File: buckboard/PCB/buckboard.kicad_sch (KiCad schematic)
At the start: 159 parts, among them J1 Conn_01x05, SW1 SW_Push, SW10 SW_Push, SW100_1.25 SW_Push, SW101 SW_Push, SW102 SW_Push, SW103_1.25 SW_Push, SW104_1.25 SW_Push, SW105_1.25 SW_Push, SW106_1.5 SW_Push, SW11 SW_Push, SW12 SW_Push, SW13 SW_Push, SW17 SW_Push, SW18 SW_Push, SW19 SW_Push, SW2 SW_Push, SW20 SW_Push, SW21 SW_Push, SW22 SW_Push, SW23 SW_Push, SW24 SW_Push, SW25 SW_Push, SW26 SW_Push, SW27 SW_Push, SW28 SW_Push, SW29 SW_Push, SW3 SW_Push, SW30_2 SW_Push, SW4 SW_Push, SW5 SW_Push, SW58_1.5 SW_Push, SW59 SW_Push, SW6 SW_Push, SW60 SW_Push, SW61 SW_Push, SW62 SW_Push, SW63 SW_Push, SW64 SW_Push, SW65 SW_Push, SW66 SW_Push, SW67 SW_Push, SW68 SW_Push, SW69 SW_Push, SW7 SW_Push, SW70 SW_Push, SW71 SW_Push, SW71_1.75 SW_Push, SW72 SW_Push, SW73 SW_Push, SW74 SW_Push, SW75 SW_Push, SW76 SW_Push, SW77 SW_Push, SW78 SW_Push, SW79 SW_Push, SW8 SW_Push, SW80 SW_Push, SW81 SW_Push, SW82 SW_Push, SW83 SW_Push, SW84_enter1 SW_Push, SW85_1.25 SW_Push, SW86 SW_Push, SW87 SW_Push, SW88 SW_Push, SW89 SW_Push, SW9 SW_Push, SW90 SW_Push, SW91 SW_Push, SW92 SW_Push, SW93 SW_Push, SW94 SW_Push, SW95 SW_Push, SW96 SW_Push, SW97_2.75 SW_Push, SW98_1.5 SW_Push, SW99_1.25 SW_Push

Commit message: created pcb model and wired it up + added secondary rotary encoder
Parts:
- added SW14: RotaryEncoder, Rotary_Encoder:RotaryEncoder_Alps_EC12E_Vertical_H20mm, symbol Device:RotaryEncoder
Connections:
- net GND: now also SW14.C
- net EC12A: now reaches A1.32 (GPIO27_ADC1)
- net EC12A: now also SW14.A
- net EC12B: now reaches A1.34 (GPIO28_ADC2)
- net EC12B: now also SW14.B
- net row1 renamed p18
- net row2 renamed p19
- net row3 renamed p20
- net row4 renamed p21
- net row5 renamed p22
- net row6 renamed p26
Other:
- moved on the sheet: OLED DISPLAY1, SWvol1

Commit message: updated pcb to have joystick module support (- 1 rotary encoder)+ gerber
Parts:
- removed SW14: RotaryEncoder, Rotary_Encoder:RotaryEncoder_Alps_EC12E_Vertical_H20mm, symbol Device:RotaryEncoder
- J1: footprint Connector_PinHeader_1.00mm:PinHeader_1x05_P1.00mm_Vertical -> Connector_PinSocket_2.00mm:PinSocket_1x05_P2.00mm_Horizontal
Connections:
- net EC12A is gone; now on net VRx: A1.32 (GPIO27_ADC1)
- net EC12B is gone; now on net VRy: A1.34 (GPIO28_ADC2)
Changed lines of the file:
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@@
 	(wire
 		(pts
-			(xy 504.19 82.55) (xy 518.16 82.55)
-		)
-		(stroke
-			(width 0)
-			(type default)
-		)
-	)
-	(wire
-		(pts
 			(xy 227.33 156.21) (xy 227.33 173.99)
 		)
@@
 		)
 	)
-	(global_label "EC12A"
-		(shape input)
-		(at 397.51 29.21 0)
-		(fields_autoplaced yes)
-		(effects
-			(font
-				(size 1.27 1.27)
-			)
-			(justify left)
-		)
-		(property "Intersheetrefs" "${INTERSHEET_REFS}"
-			(at 406.4218 29.21 0)
-			(hide yes)
-			(show_name no)
-			(do_not_autoplace no)
-			(effects
-				(font
-					(size 1.27 1.27)
-				)
-				(justify left)
-			)
-		)
-	)
 	(global_label "row4"
 		(shape input)
@@
 		)
 	)
+	(global_label "VRy"
+		(shape input)
+		(at 397.51 31.75 0)
+		(fields_autoplaced yes)
+		(effects
+			(font
+				(size 1.27 1.27)
+			)
+			(justify left)
+		)
+		(property "Intersheetrefs" "${INTERSHEET_REFS}"
+			(at 403.8214 31.75 0)
+			(hide yes)
+			(show_name no)
+			(do_not_autoplace no)
+			(effects
+				(font
+					(size 1.27 1.27)
+				)
+				(justify left)
+			)
+		)
+	)
 	(global_label "p18"
 		(shape input)
@@
 		)
 	)
-	(global_label "EC12A"
-		(shape input)
-		(at 518.16 80.01 180)
-		(fields_autoplaced yes)
-		(effects
-			(font
-				(size 1.27 1.27)
-			)
-			(justify right)
-		)
-		(property "Intersheetrefs" "${INTERSHEET_REFS}"
-			(at 509.2482 80.01 0)
-			(hide yes)
-			(show_name no)
-			(do_not_autoplace no)
-			(effects
-				(font
-					(size 1.27 1.27)
-				)
-				(justify right)
-			)
-		)
-	)
 	(global_label "col10"
 		(shape input)
@@
 		)
 	)
-	(global_label "EC12B"
-		(shape input)
-		(at 518.16 85.09 180)
-		(fields_autoplaced yes)
-		(effects
-			(font
-				(size 1.27 1.27)
-			)
-			(justify right)
-		)
-		(property "Intersheetrefs" "${INTERSHEET_REFS}"
-			(at 509.0668 85.09 0)
-			(hide yes)
-			(show_name no)
-			(do_not_autoplace no)
-			(effects
-				(font
-					(size 1.27 1.27)
-				)
-				(justify right)
-			)
-		)
-	)
 	(global_label "col3"
 		(shape input)
@@
 		)
 	)
+	(global_label "VRx"
+		(shape input)
+		(at 397.51 29.21 0)
+		(fields_autoplaced yes)
+		(effects
+			(font
+				(size 1.27 1.27)
+			)
+			(justify left)
+		)
+		(property "Intersheetrefs" "${INTERSHEET_REFS}"
+			(at 403.8819 29.21 0)
+			(hide yes)
+			(show_name no)
+			(do_not_autoplace no)
+			(effects
+				(font
+					(size 1.27 1.27)
+				)
+				(justify left)
+			)
+		)
+	)
 	(global_label "col2"
 		(shape input)
@@
 		)
 	)
-	(global_label "EC12B"
-		(shape input)
-		(at 397.51 31.75 0)
-		(fields_autoplaced yes)
-		(effects
-			(font
-				(size 1.27 1.27)
-			)
-			(justify left)
-		)
-		(property "Intersheetrefs" "${INTERSHEET_REFS}"
-			(at 406.6032 31.75 0)
-			(hide yes)
-			(show_name no)
-			(do_not_autoplace no)
-			(effects
-				(font
-					(size 1.27 1.27)
-				)
-				(justify left)
-			)
-		)
-	)
 	(global_label "col14"
 		(shape input)
@@
 	)
 	(symbol
-		(lib_id "power:GND")
-		(at 504.19 82.55 0)
-		(unit 1)
-		(body_style 1)
-		(exclude_from_sim no)
-		(in_bom yes)
-		(on_board yes)
-		(in_pos_files yes)
-		(dnp no)
-		(fields_autoplaced yes)
-		(property "Reference" "#PWR09"
-			(at 504.19 88.9 0)
-			(hide yes)
-			(show_name no)
-			(do_not_autoplace no)
-			(effects
-				(font
-					(size 1.27 1.27)
-				)
-			)
-		)
-		(property "Value" "GND"
-			(at 504.19 87.63 0)
-			(show_name no)
-			(do_not_autoplace no)
-			(effects
-				(font
-					(size 1.27 1.27)
-				)
-			)
-		)
-		(property "Footprint" ""
-			(at 504.19 82.55 0)
-			(hide yes)
-			(show_name no)
-			(do_not_autoplace no)
-			(effects
-				(font
-					(size 1.27 1.27)
-				)
-			)
-		)
-		(property "Datasheet" ""
-			(at 504.19 82.55 0)
-			(hide yes)
-			(show_name no)
-			(do_not_autoplace no)
-			(effects
-				(font
-					(size 1.27 1.27)
-				)
-			)
-		)
-		(property "Description" "Power symbol creates a global label with name \"GND\" , ground"
-			(at 504.19 82.55 0)
-			(hide yes)
-			(show_name no)
-			(do_not_autoplace no)
-			(effects
-				(font
-					(size 1.27 1.27)
-				)
-			)
-		)
-		(pin "1"
-		)
-		(instances
-			(project "buckboard"
-				(path "/92392aa8-3793-4fda-a137-246c9c5a2323"
-					(reference "#PWR09")
-					(unit 1)
-				)
-			)
-		)
-	)
-	(symbol
 		(lib_id "Switch:SW_Push")
 		(at 278.13 80.01 180)
@@
 	)
 	(symbol
-		(lib_id "Device:RotaryEncoder")
-		(at 525.78 82.55 0)
-		(unit 1)
-		(body_style 1)
-		(exclude_from_sim no)
-		(in_bom yes)
-		(on_board yes)
-		(in_pos_files yes)
-		(dnp no)
-		(fields_autoplaced yes)
-		(property "Reference" "SW14"
-			(at 532.13 81.2799 0)
-			(show_name no)
-			(do_not_autoplace no)
-			(effects
-				(font
-					(size 1.27 1.27)
-				)
-				(justify left)
-			)
-		)
-		(property "Value" "RotaryEncoder"
-			(at 532.13 83.8199 0)
-			(show_name no)
-			(do_not_autoplace no)
-			(effects
-				(font
-					(size 1.27 1.27)
-				)
-				(justify left)
-			)
-		)
-		(property "Footprint" "Rotary_Encoder:RotaryEncoder_Alps_EC12E_Vertical_H20mm"
-			(at 521.97 78.486 0)
-			(hide yes)
-			(show_name no)
-			(do_not_autoplace no)
-			(effects
-				(font
-					(size 1.27 1.27)
-				)
-			)
-		)
-		(property "Datasheet" ""
-			(at 525.78 75.946 0)
-			(hide yes)
-			(show_name no)
-			(do_not_autoplace no)
-			(effects
-				(font
-					(size 1.27 1.27)
-				)
-			)
-		)
-		(property "Description" "Rotary encoder, dual channel, incremental quadrate outputs"
-			(at 525.78 82.55 0)
-			(hide yes)
-			(show_name no)
-			(do_not_autoplace no)
-			(effects
-				(font
-					(size 1.27 1.27)
-				)
-			)
-		)
-		(pin "C"
-		)
-		(pin "B"
-		)
-		(pin "A"
-		)
-		(instances
-			(project "buckboard"
-				(path "/92392aa8-3793-4fda-a137-246c9c5a2323"
-					(reference "SW14")
-					(unit 1)
-				)
-			)
-		)
-	)
-	(symbol
 		(lib_id "Switch:SW_Push")
 		(at 293.37 80.01 180)
@@
 			)
 		)
-		(property "Footprint" "Connector_PinHeader_1.00mm:PinHeader_1x05_P1.00mm_Vertical"
+		(property "Footprint" "Connector_PinSocket_2.00mm:PinSocket_1x05_P2.00mm_Horizontal"
 			(at 535.94 161.29 0)
 			(hide yes)

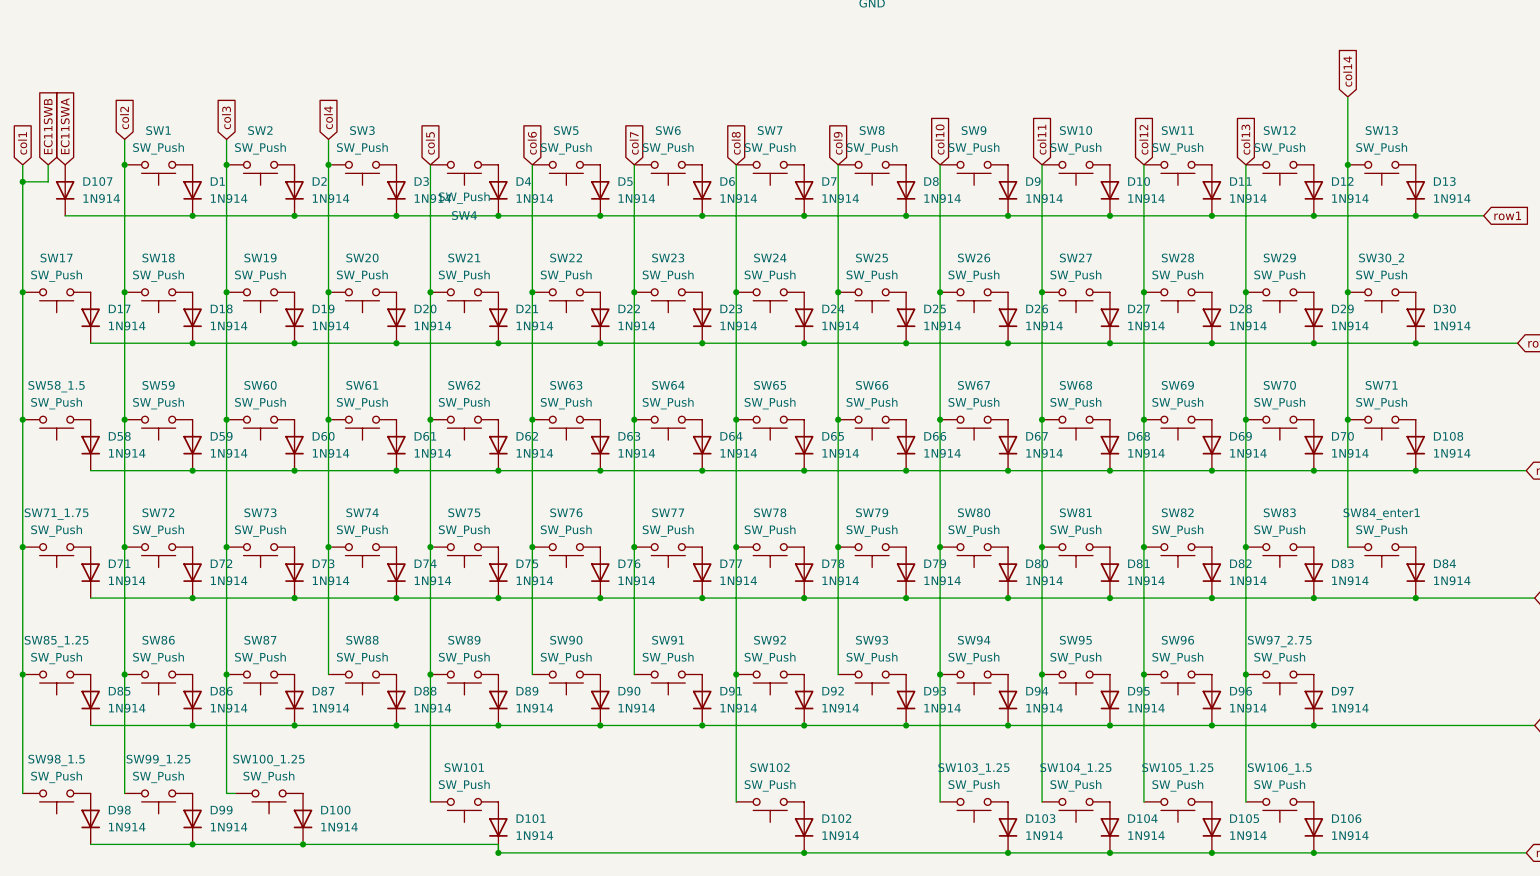
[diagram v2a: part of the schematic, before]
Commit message: added firmware to the repo (still not working)
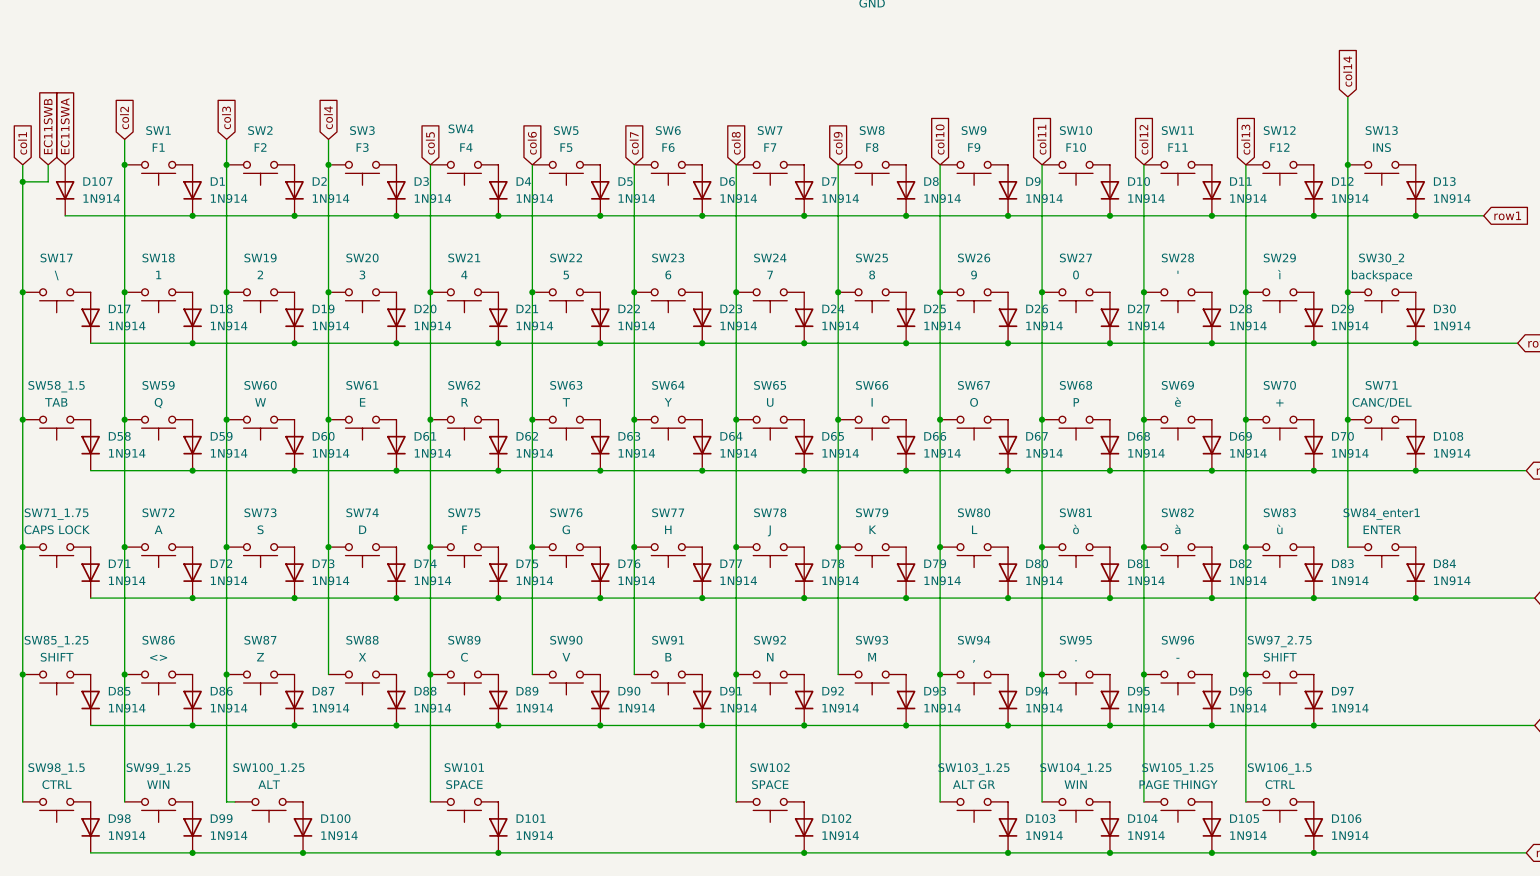
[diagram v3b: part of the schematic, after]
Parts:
- SW1: value SW_Push -> F1
- SW10: value SW_Push -> F10
- SW100_1.25: value SW_Push -> ALT
- SW101, SW102: value SW_Push -> SPACE
- SW103_1.25: value SW_Push -> ALT GR
- SW104_1.25, SW99_1.25: value SW_Push -> WIN
- SW105_1.25: value SW_Push -> PAGE THINGY
- SW106_1.5, SW98_1.5: value SW_Push -> CTRL
- SW11: value SW_Push -> F11
- SW12: value SW_Push -> F12
- SW13: value SW_Push -> INS
- SW17: value SW_Push -> \
- SW18: value SW_Push -> 1
- SW19: value SW_Push -> 2
- SW2: value SW_Push -> F2
- SW20: value SW_Push -> 3
- SW21: value SW_Push -> 4
- SW22: value SW_Push -> 5
- SW23: value SW_Push -> 6
- SW24: value SW_Push -> 7
- SW25: value SW_Push -> 8
- SW26: value SW_Push -> 9
- SW27: value SW_Push -> 0
- SW28: value SW_Push -> '
- SW29: value SW_Push -> ì
- SW3: value SW_Push -> F3
- SW30_2: value SW_Push -> backspace
- SW4: value SW_Push -> F4
- SW5: value SW_Push -> F5
- SW58_1.5: value SW_Push -> TAB
- SW59: value SW_Push -> Q
- SW6: value SW_Push -> F6
- SW60: value SW_Push -> W
- SW61: value SW_Push -> E
- SW62: value SW_Push -> R
- SW63: value SW_Push -> T
- SW64: value SW_Push -> Y
- SW65: value SW_Push -> U
- SW66: value SW_Push -> I
- SW67: value SW_Push -> O
- SW68: value SW_Push -> P
- SW69: value SW_Push -> è
- SW7: value SW_Push -> F7
- SW70: value SW_Push -> +
- SW71: value SW_Push -> CANC/DEL
- SW71_1.75: value SW_Push -> CAPS LOCK
- SW72: value SW_Push -> A
- SW73: value SW_Push -> S
- SW74: value SW_Push -> D
- SW75: value SW_Push -> F
- SW76: value SW_Push -> G
- SW77: value SW_Push -> H
- SW78: value SW_Push -> J
- SW79: value SW_Push -> K
- SW8: value SW_Push -> F8
- SW80: value SW_Push -> L
- SW81: value SW_Push -> ò
- SW82: value SW_Push -> à
- SW83: value SW_Push -> ù
- SW84_enter1: value SW_Push -> ENTER
- SW85_1.25, SW97_2.75: value SW_Push -> SHIFT
- SW86: value SW_Push -> <>
- SW87: value SW_Push -> Z
- SW88: value SW_Push -> X
- SW89: value SW_Push -> C
- SW9: value SW_Push -> F9
- SW90: value SW_Push -> V
- SW91: value SW_Push -> B
- SW92: value SW_Push -> N
- SW93: value SW_Push -> M
- SW94: value SW_Push -> ,
- SW95: value SW_Push -> .
- SW96: value SW_Push -> -
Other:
- moved on the sheet: D100, D98, D99, SW100_1.25, SW98_1.5, SW99_1.25
